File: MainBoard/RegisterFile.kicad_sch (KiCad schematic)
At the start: 4 parts, among them U27 IDT7024L15PFG, U28 IDT7024L15PFG

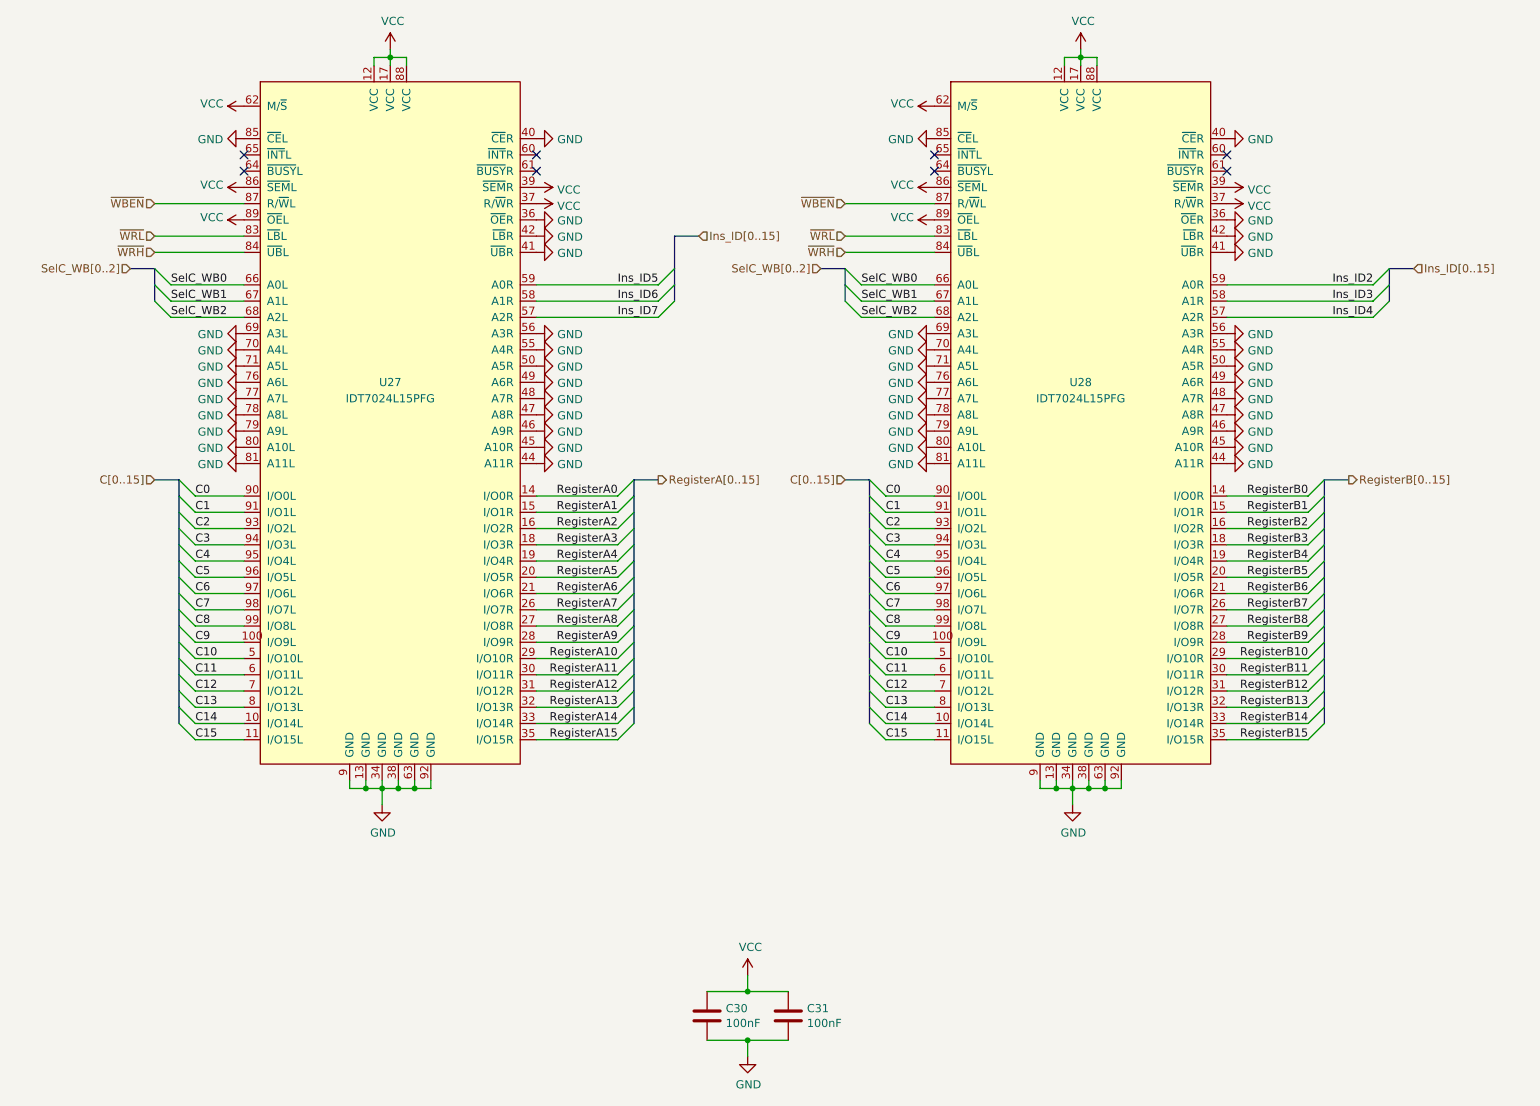
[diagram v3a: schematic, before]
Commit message: MainBoard: Update schematic to sync with MEMModule, Rev B
Unroute the PCB layout. Update the schematic to include changes from
revision B of MEMModule. This includes changes to put instruction ROM on
the PCB again.
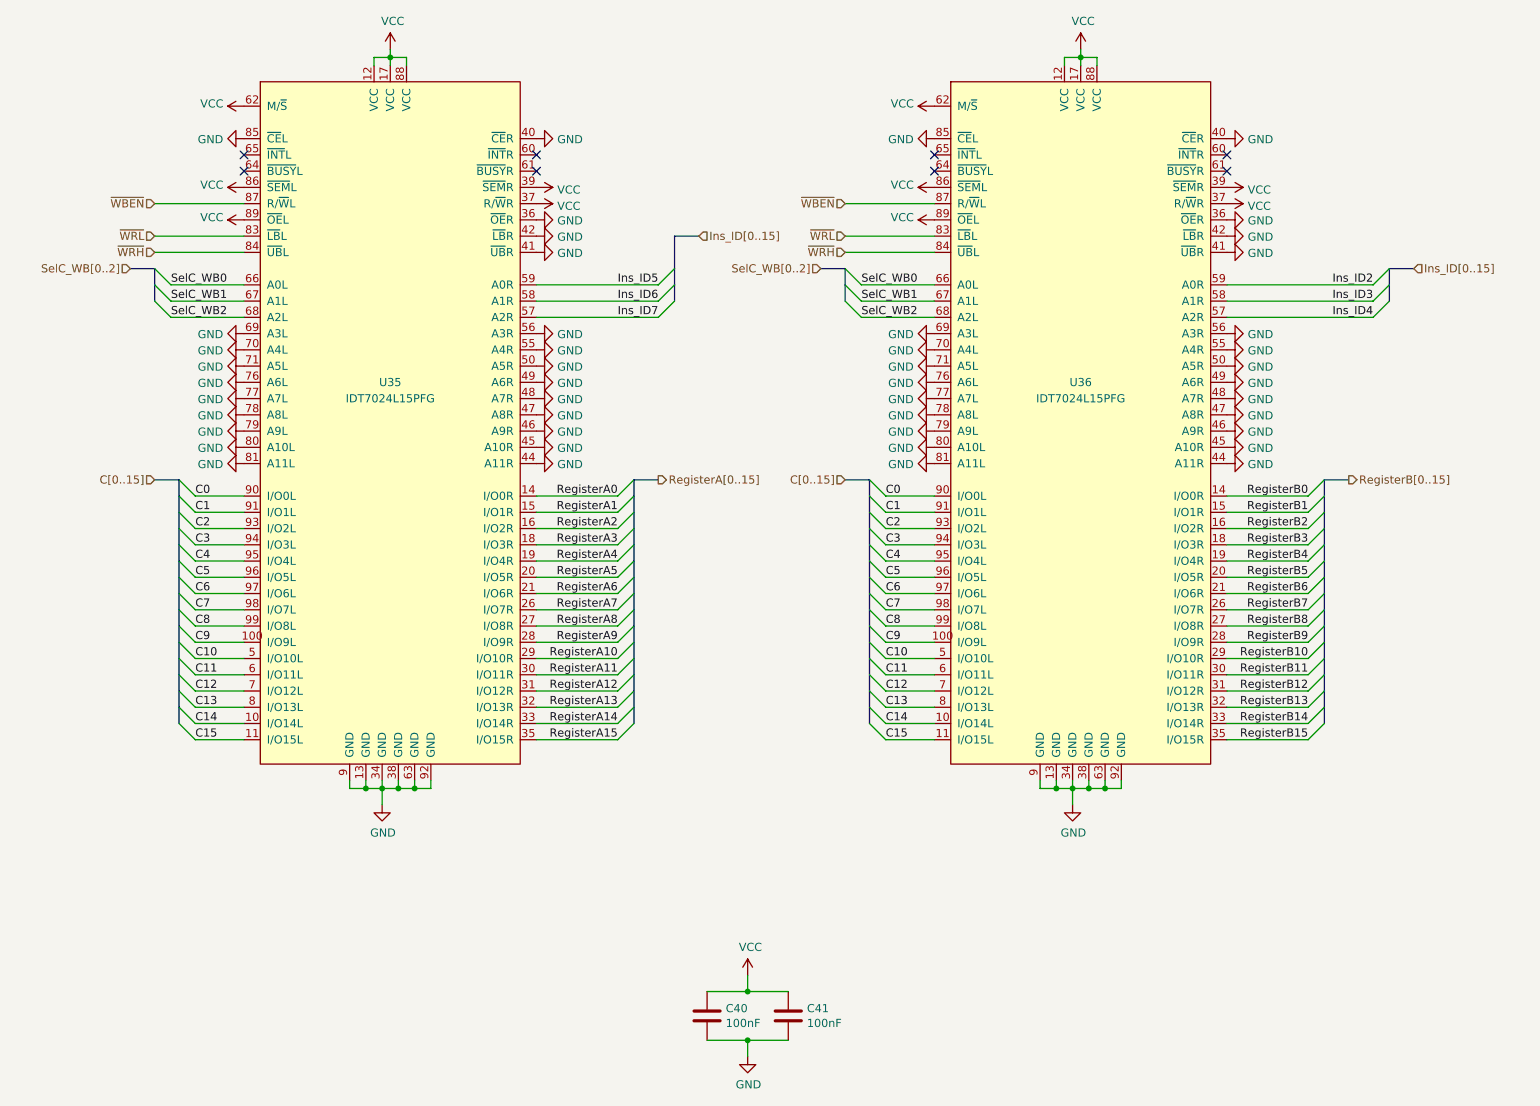
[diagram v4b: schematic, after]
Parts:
- renumbered C30 to C40, C31 to C41, U27 to U35, U28 to U36

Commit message: Update schematics for the MainBoard to include the ControleModule fix from 704c0dce
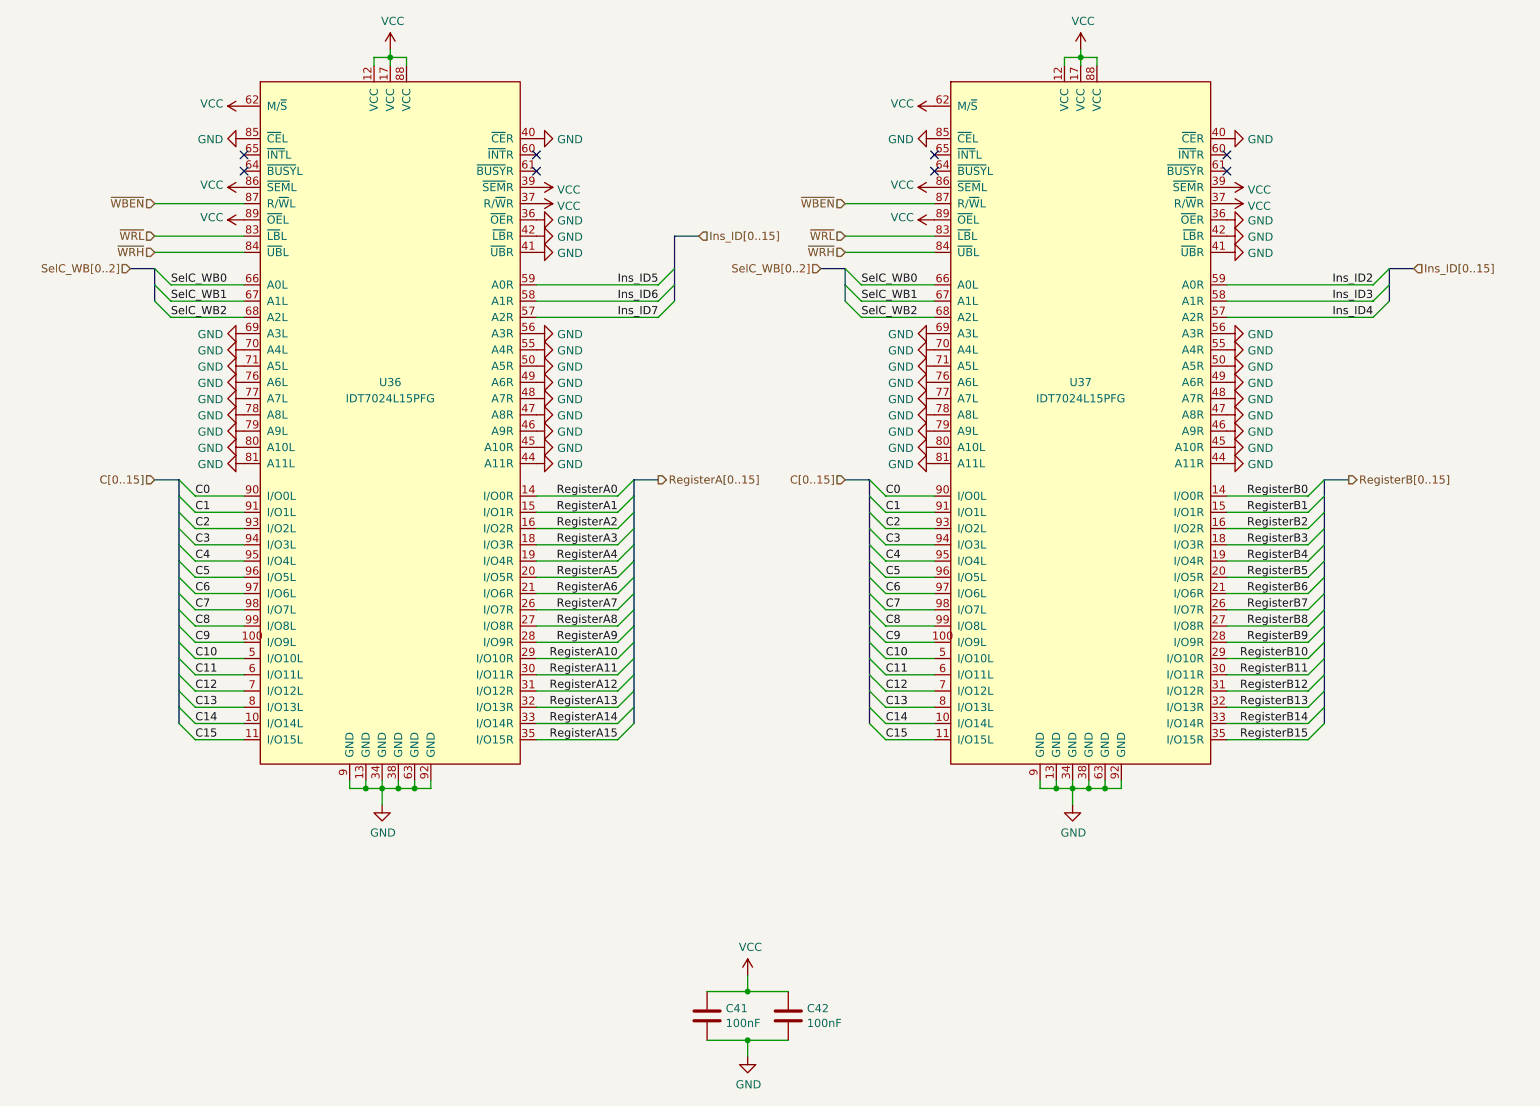
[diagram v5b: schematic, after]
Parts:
- renumbered C40 to C41, C41 to C42, U35 to U36, U36 to U37

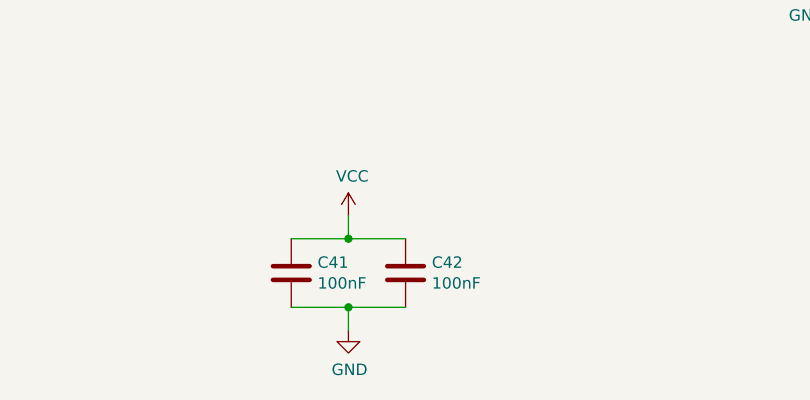
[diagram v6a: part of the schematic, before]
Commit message: MainBoard: Relabel capacitors from 100nF to 0.1uF
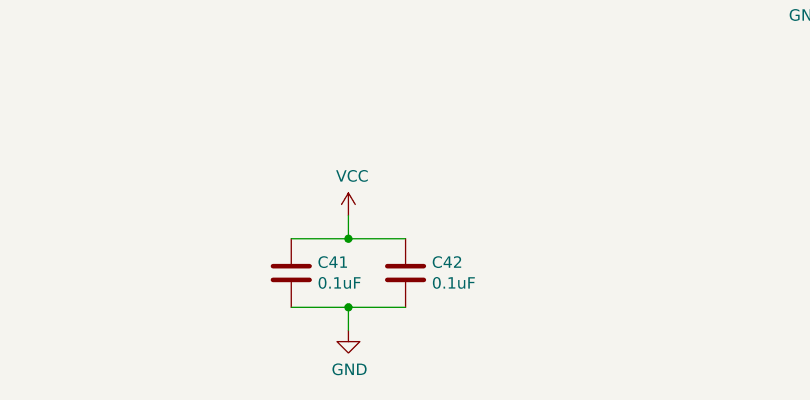
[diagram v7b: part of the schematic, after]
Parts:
- C41, C42: value 100nF -> 0.1uF
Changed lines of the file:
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@@
       (effects (font (size 1.27 1.27)) (justify left))
     )
-    (property "Value" "100nF" (at 152.781 191.643 0)
+    (property "Value" "0.1uF" (at 152.781 191.643 0)
       (effects (font (size 1.27 1.27)) (justify left))
     )
@@
       (effects (font (size 1.27 1.27)) (justify left))
     )
-    (property "Value" "100nF" (at 140.081 191.643 0)
+    (property "Value" "0.1uF" (at 140.081 191.643 0)
       (effects (font (size 1.27 1.27)) (justify left))
     )

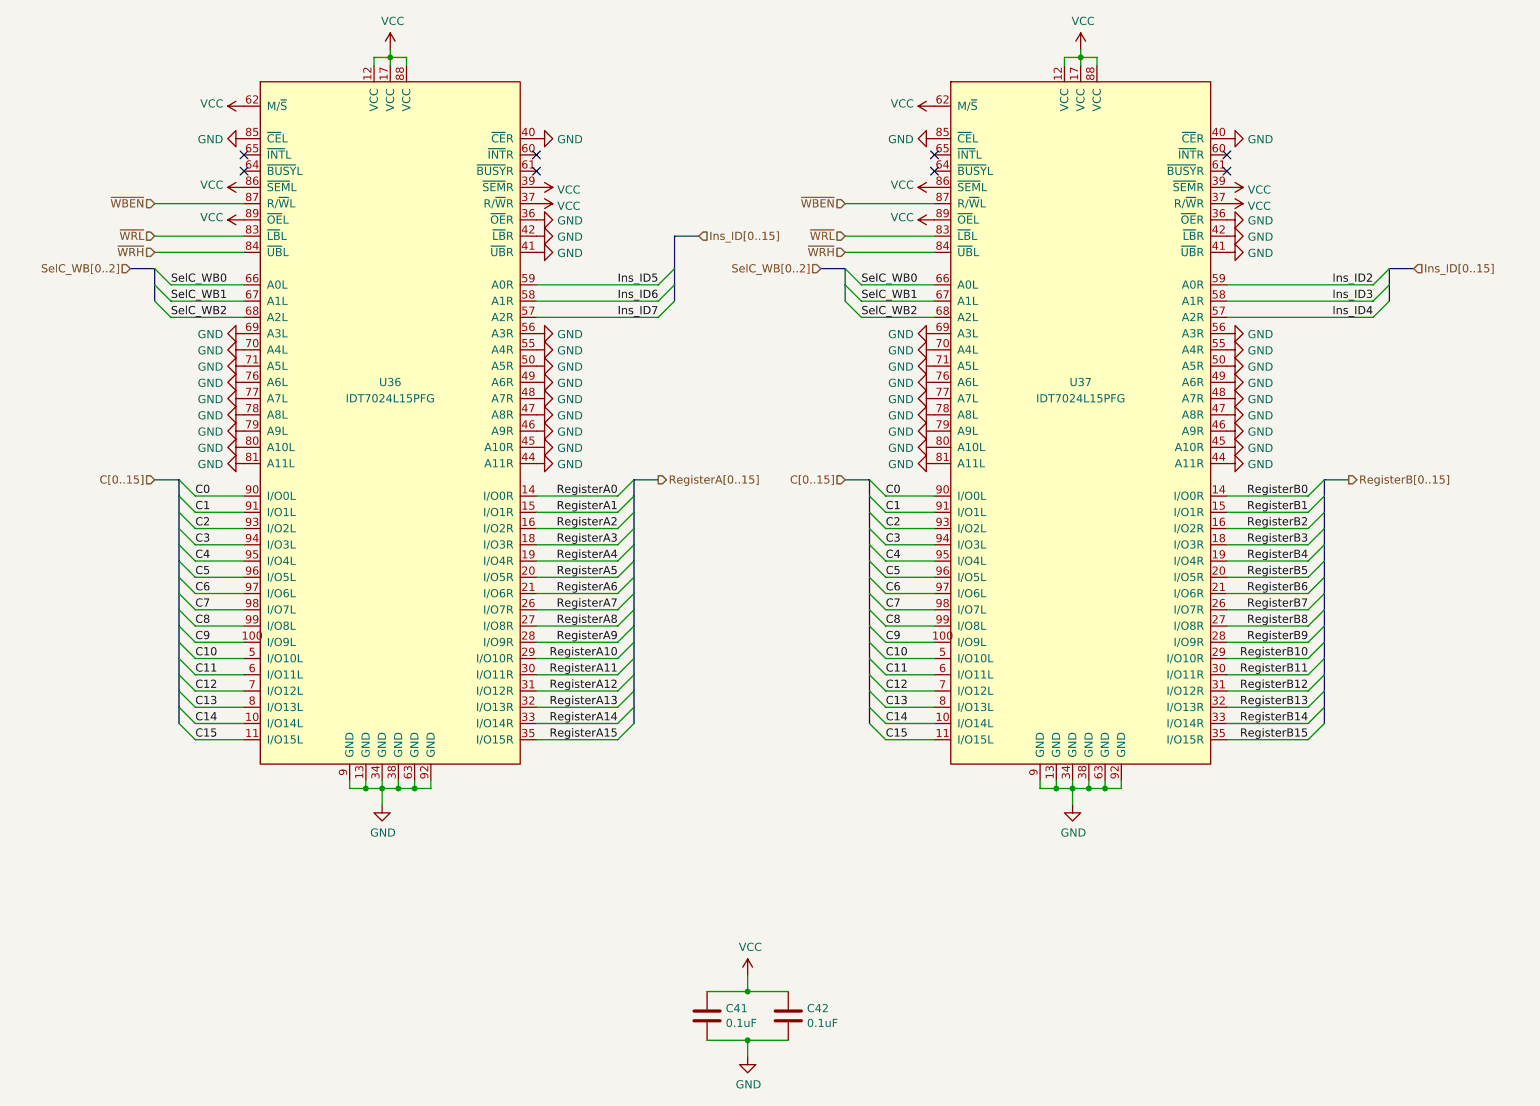
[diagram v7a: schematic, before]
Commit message: MainBoard: update schematic with latest changes to the clock
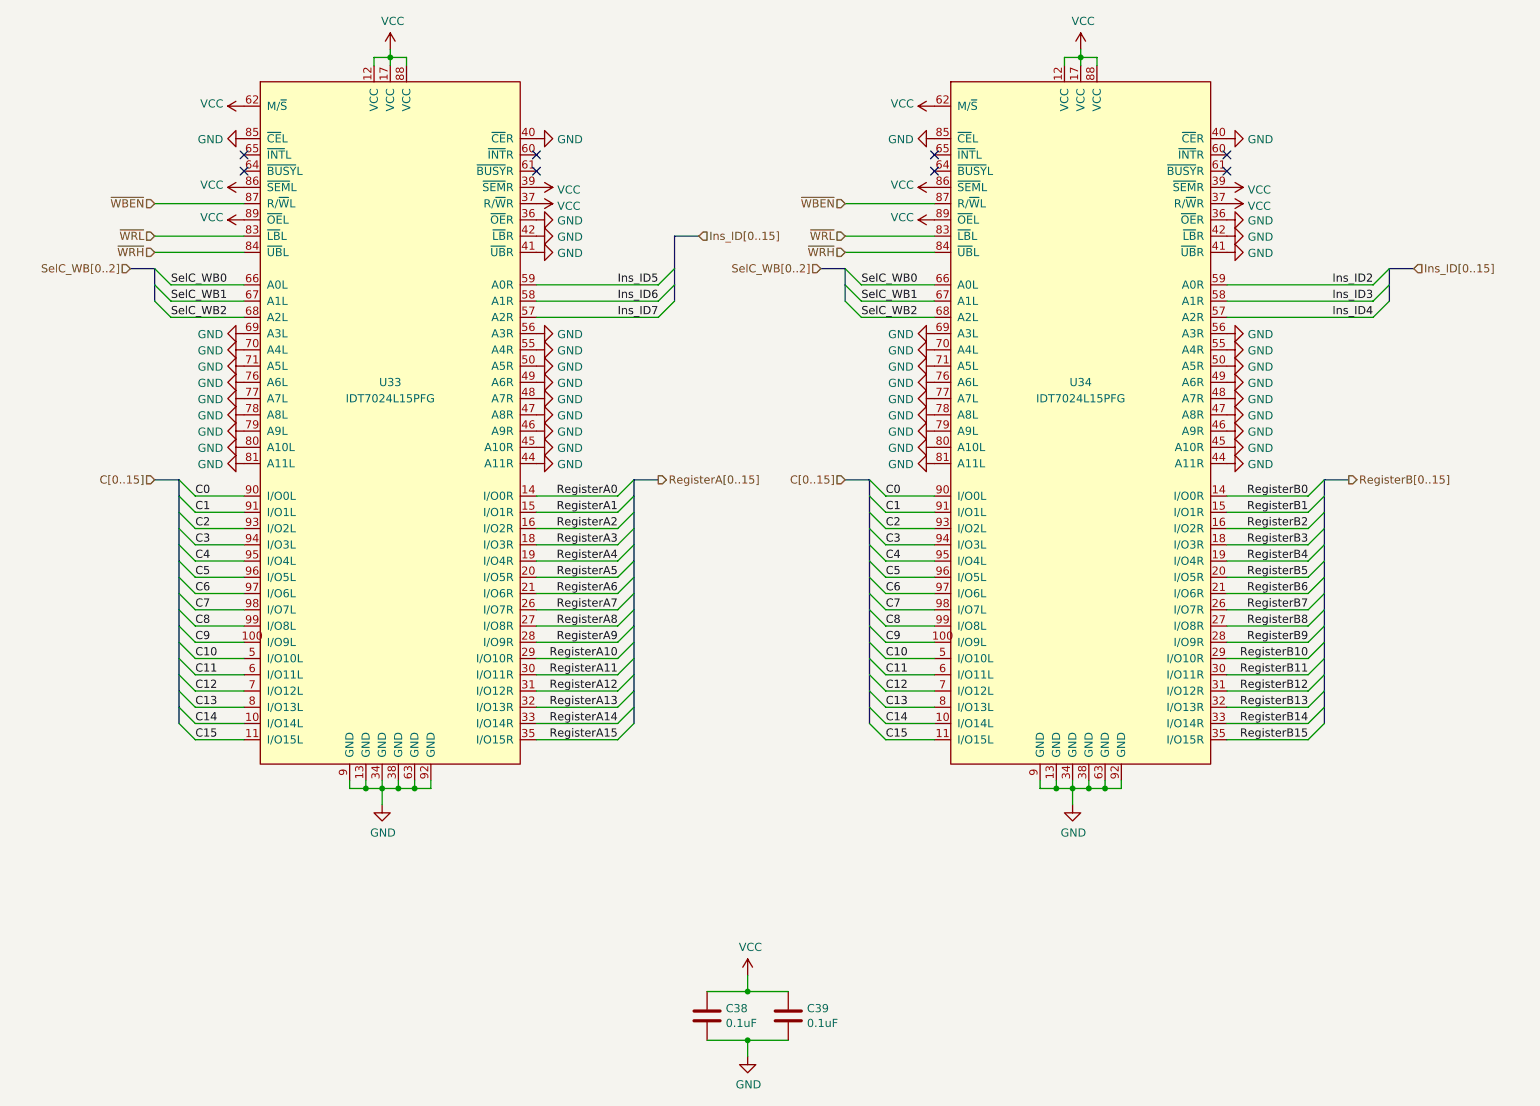
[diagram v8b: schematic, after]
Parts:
- renumbered C41 to C38, C42 to C39, U36 to U33, U37 to U34
